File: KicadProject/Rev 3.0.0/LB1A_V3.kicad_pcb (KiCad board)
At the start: 6 copper layers, 45 x 45 mm, 194 parts, among them J601 2337019-1, J602 2337019-1, U101 LFBGA448_18X18, U201 AS4C256M16D3LC-12BCN, U401 STPMIC1xPQR, U501 S40FC004C1B2C00000, U601 LBEE59B1LV-278, U701 DF40C-100DP-0.4V(51), U702 DF40C-100DP-0.4V(51), U703 DF40C-100DP-0.4V(51), X101 32.768kHz, Y101 24MHz

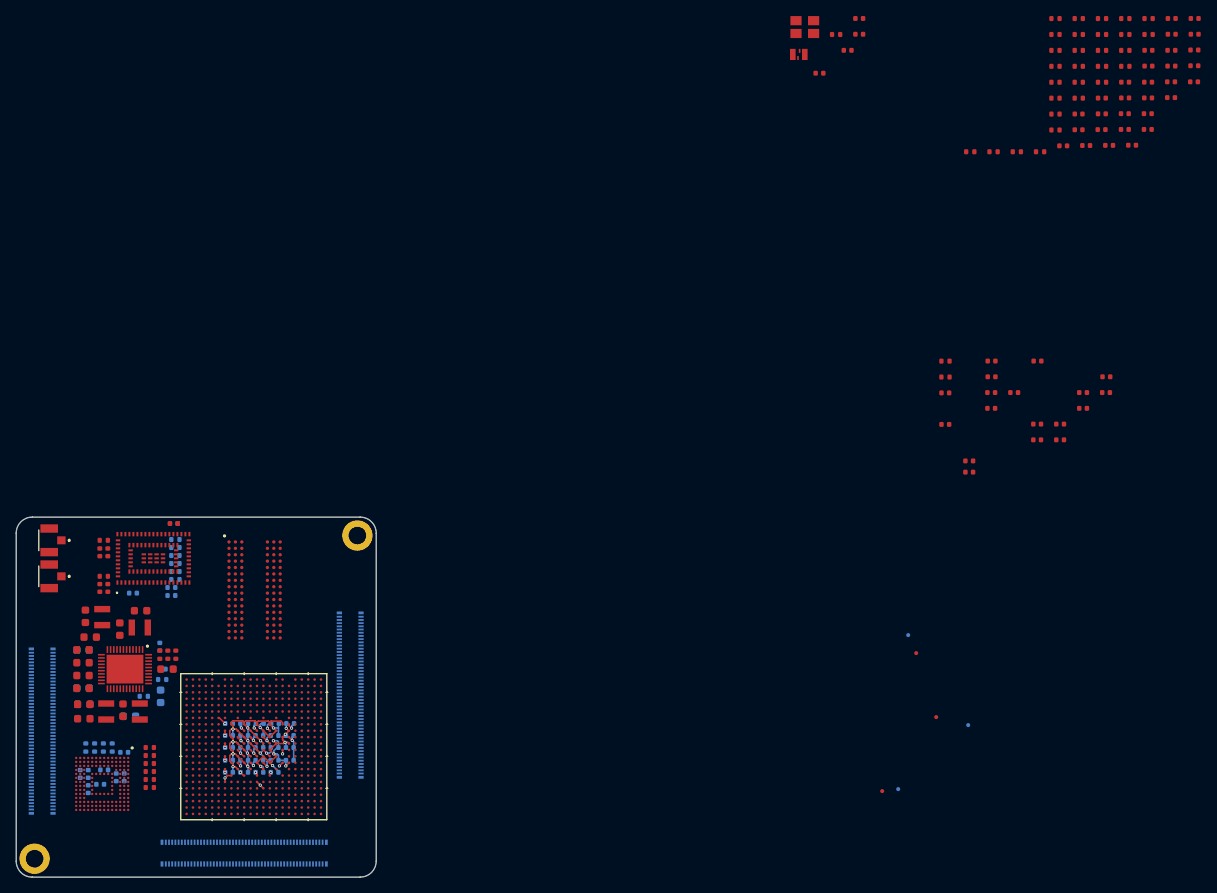
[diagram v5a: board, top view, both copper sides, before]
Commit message: mpu vdd_ddq done
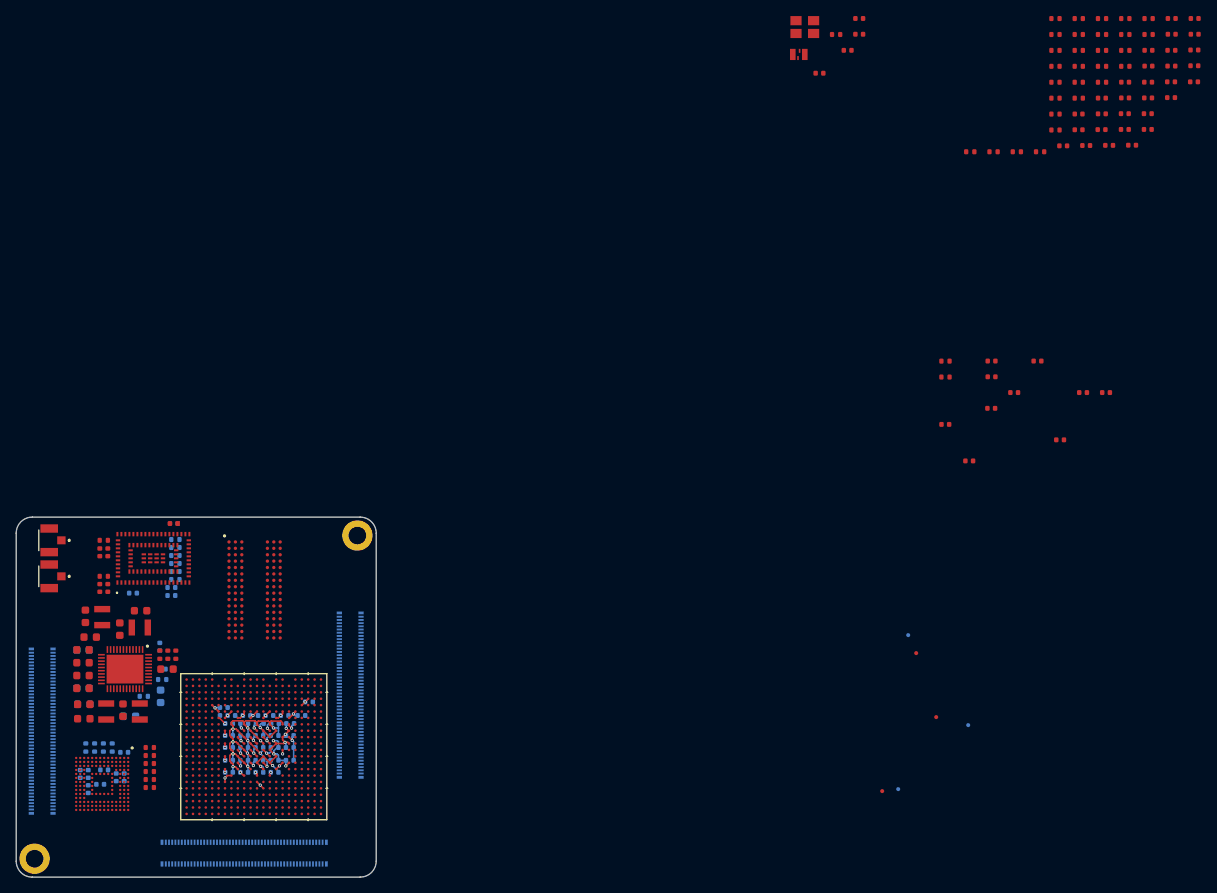
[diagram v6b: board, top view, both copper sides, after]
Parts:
- C331, C332, C333, C334, C338, C339, C340, C341: moved to B.Cu
- moved C341 117.8 mm to (126.0, 108.8)
- moved C338 110.5 mm to (129.8, 109.8)
- moved C339 108.9 mm to (127.8, 109.8), turned to 180 degrees
- moved C340 107.4 mm to (126.0, 109.8), turned to 180 degrees
- moved C333 100.9 mm to (133.6, 109.8)
- moved C334 98.8 mm to (131.7, 109.8)
- moved C332 90.0 mm to (135.7, 109.8)
- moved C331 87.4 mm to (136.6, 108.1)
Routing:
- net PMIC_VOUT2_VDD_DDR: track 0.00 -> 11.1 mm, vias 0 -> 8
- net GND: track 32.0 -> 32.6 mm

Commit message: mpu another commit
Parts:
- removed C318: 1uF, U_Capacitor_SMD:C_0402_1005Metric
- removed C319: 10nF, U_Capacitor_SMD:C_0402_1005Metric
- removed C320: 100nF, U_Capacitor_SMD:C_0402_1005Metric
- C317, C325, C330, C335, C336, C337, C342, R301, R302: moved to B.Cu
- U101: value LFBGA448_18X18 -> STM32MP157CAA3
- moved C342 117.7 mm to (122.2, 108.1)
- moved C336 108.9 mm to (122.2, 111.3)
- moved C317 108.6 mm to (128.1, 119.0), turned to 90 degrees
- moved C337 107.8 mm to (137.2, 111.9), turned to 180 degrees
- moved R301 101.9 mm to (129.4, 119.0), turned to 90 degrees
- moved C335 100.6 mm to (137.2, 112.9), turned to 180 degrees
- moved R302 100.0 mm to (130.5, 119.0), turned to 90 degrees
- moved C325 94.6 mm to (132.7, 117.9), turned to 180 degrees
- moved C330 94.5 mm to (137.7, 108.4), turned to 90 degrees
- moved R101 81.0 mm to (132.4, 65.3)
- moved C102 81.0 mm to (135.3, 63.3)
- moved C103 81.0 mm to (130.3, 70.1)
- moved C104 81.0 mm to (133.8, 67.2)
- moved C105 81.0 mm to (135.3, 65.2)
- moved X101 81.0 mm to (127.7, 67.8)
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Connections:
- C325 pad 2: PMIC_VOUT4_3V3 -> VDDA
- U101 pad P6: PMIC_VOUT4_3V3 -> VDDA
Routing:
- net VDDA: track 0.00 -> 0.51 mm, vias 0 -> 1

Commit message: mpu done
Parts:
- C104, C105, X101: moved to B.Cu
- moved C102 60.8 mm to (135.3, 124.1), turned to 180 degrees
- moved Y101 60.7 mm to (132.3, 124.9), turned to 180 degrees
- moved C105 58.5 mm to (132.8, 123.7), turned to 270 degrees
- moved C104 56.4 mm to (131.6, 123.7), turned to 270 degrees
- moved X101 55.8 mm to (129.7, 123.5)
- moved C103 55.2 mm to (129.6, 125.3), turned to 270 degrees
- moved R101 43.7 mm to (139.8, 108.3), turned to 90 degrees
- moved U701 2.25 mm to (126.2, 127.1)
